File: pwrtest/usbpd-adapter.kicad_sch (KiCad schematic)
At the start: 11 parts, among them J3 USB_C_Receptacle_USB2.0_16P, Q1 AO3400A, U3 IP2721

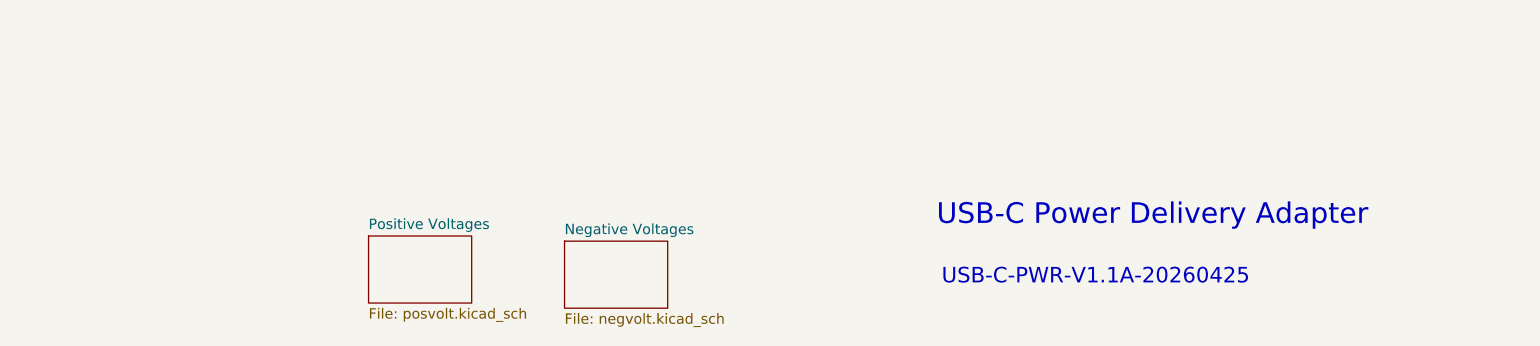
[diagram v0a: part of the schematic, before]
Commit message: adding undervoltage detection circuits
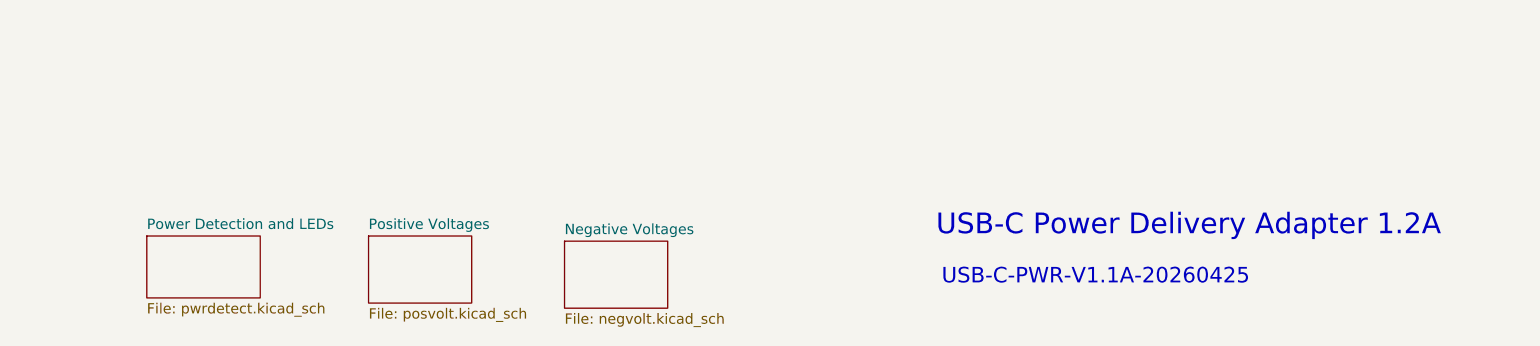
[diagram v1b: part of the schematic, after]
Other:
- added sheet Power Detection and LEDs (pwrdetect.kicad_sch)
- note added: "USB-C Power Delivery Adapter 1.2A"
- note removed: "USB-C Power Delivery Adapter"
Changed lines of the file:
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@@
 	(generator_version "10.0")
 	(paper "A4")
-	(text "USB-C Power Delivery Adapter\n"
-		(exclude_from_sim no)
-		(at 213.995 170.18 0)
+	(text "USB-C Power Delivery Adapter 1.2A\n"
+		(exclude_from_sim no)
+		(at 218.44 171.45 0)
 		(effects
 			(font
@@
 				)
 			)
+		)
+	)
+	(sheet
+		(at 90.17 172.72)
+		(size 13.97 7.62)
+		(exclude_from_sim no)
+		(in_bom yes)
+		(on_board yes)
+		(dnp no)
+		(fields_autoplaced yes)
+		(stroke
+			(width 0.1524)
+			(type solid)
+		)
+		(fill
+			(color 0 0 0 0)
+		)
+		(property "Sheetname" "Power Detection and LEDs"
+			(at 90.17 172.0084 0)
+			(show_name no)
+			(do_not_autoplace no)
+			(effects
+				(font
+					(size 1.27 1.27)
+				)
+				(justify left bottom)
+			)
+		)
+		(property "Sheetfile" "pwrdetect.kicad_sch"
+			(at 90.17 180.9246 0)
+			(show_name no)
+			(do_not_autoplace no)
+			(effects
+				(font
+					(size 1.27 1.27)
+				)
+				(justify left top)
+			)
+		)
+		(instances
+			(project "usbpd-adapter"
+				(path "/4a647462-7ef8-4ca9-abe7-1697e001dd97"
+					(page "4")
+				)
+			)

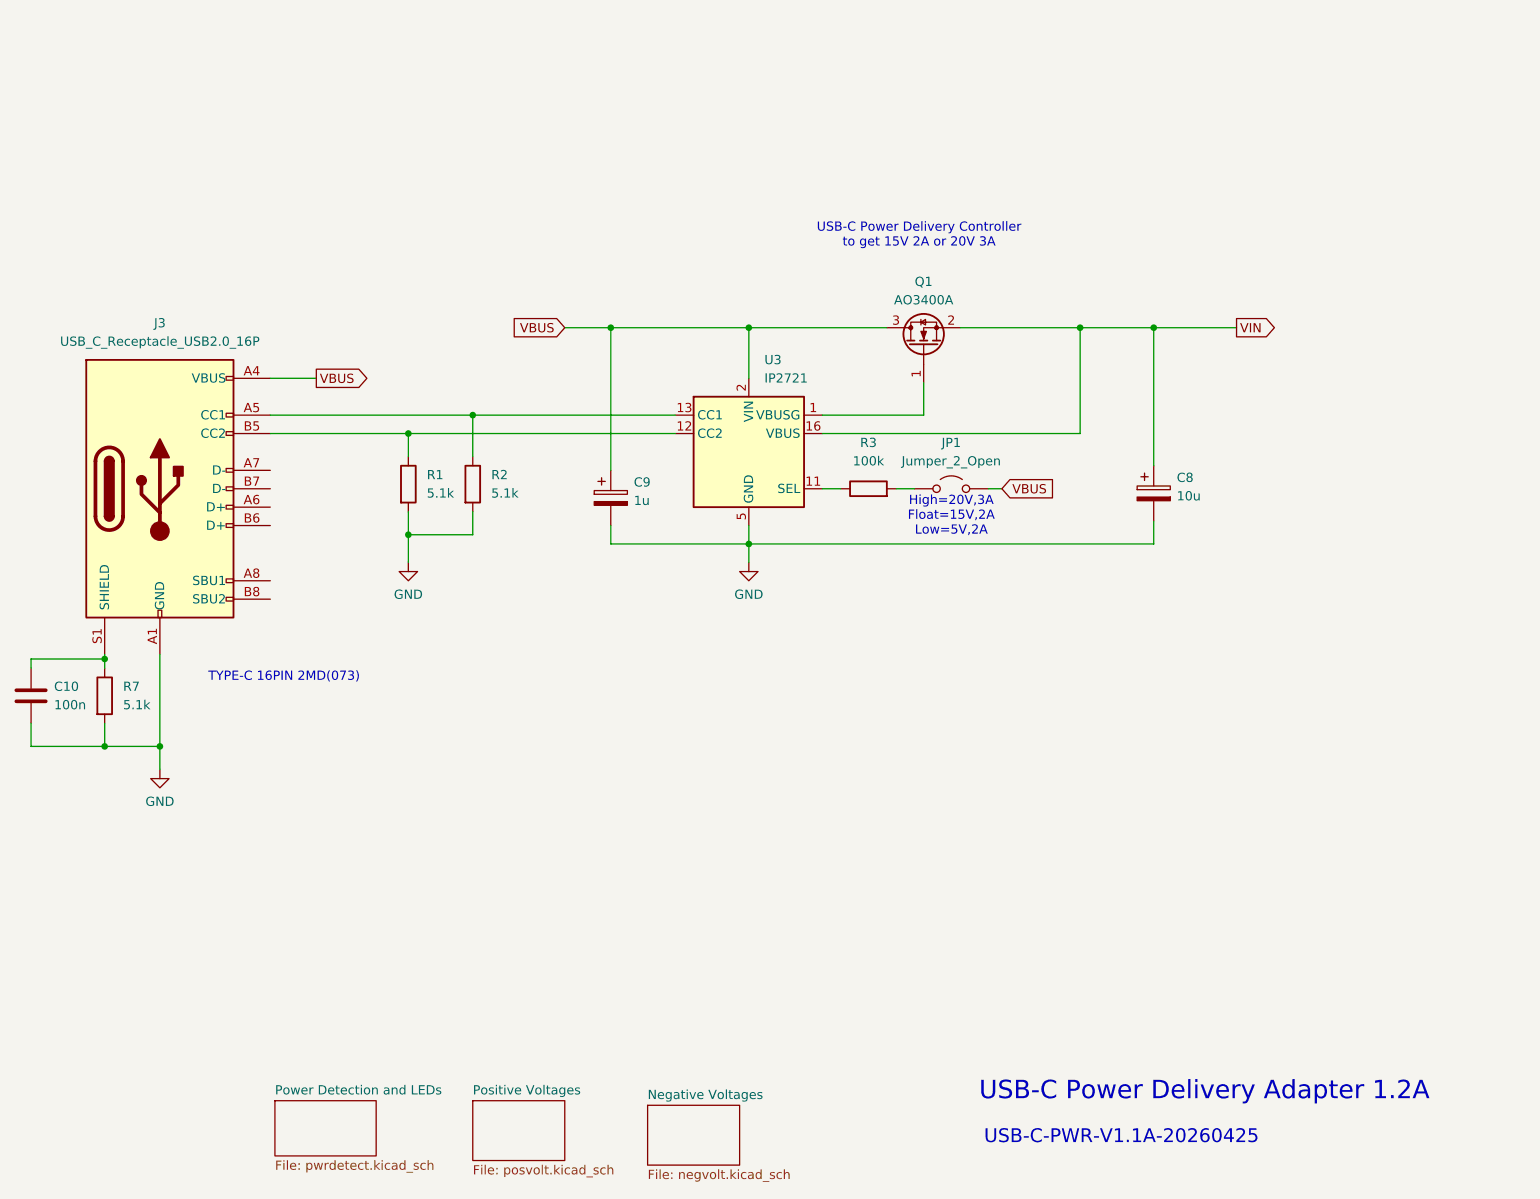
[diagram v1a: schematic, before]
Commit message: new usb controller
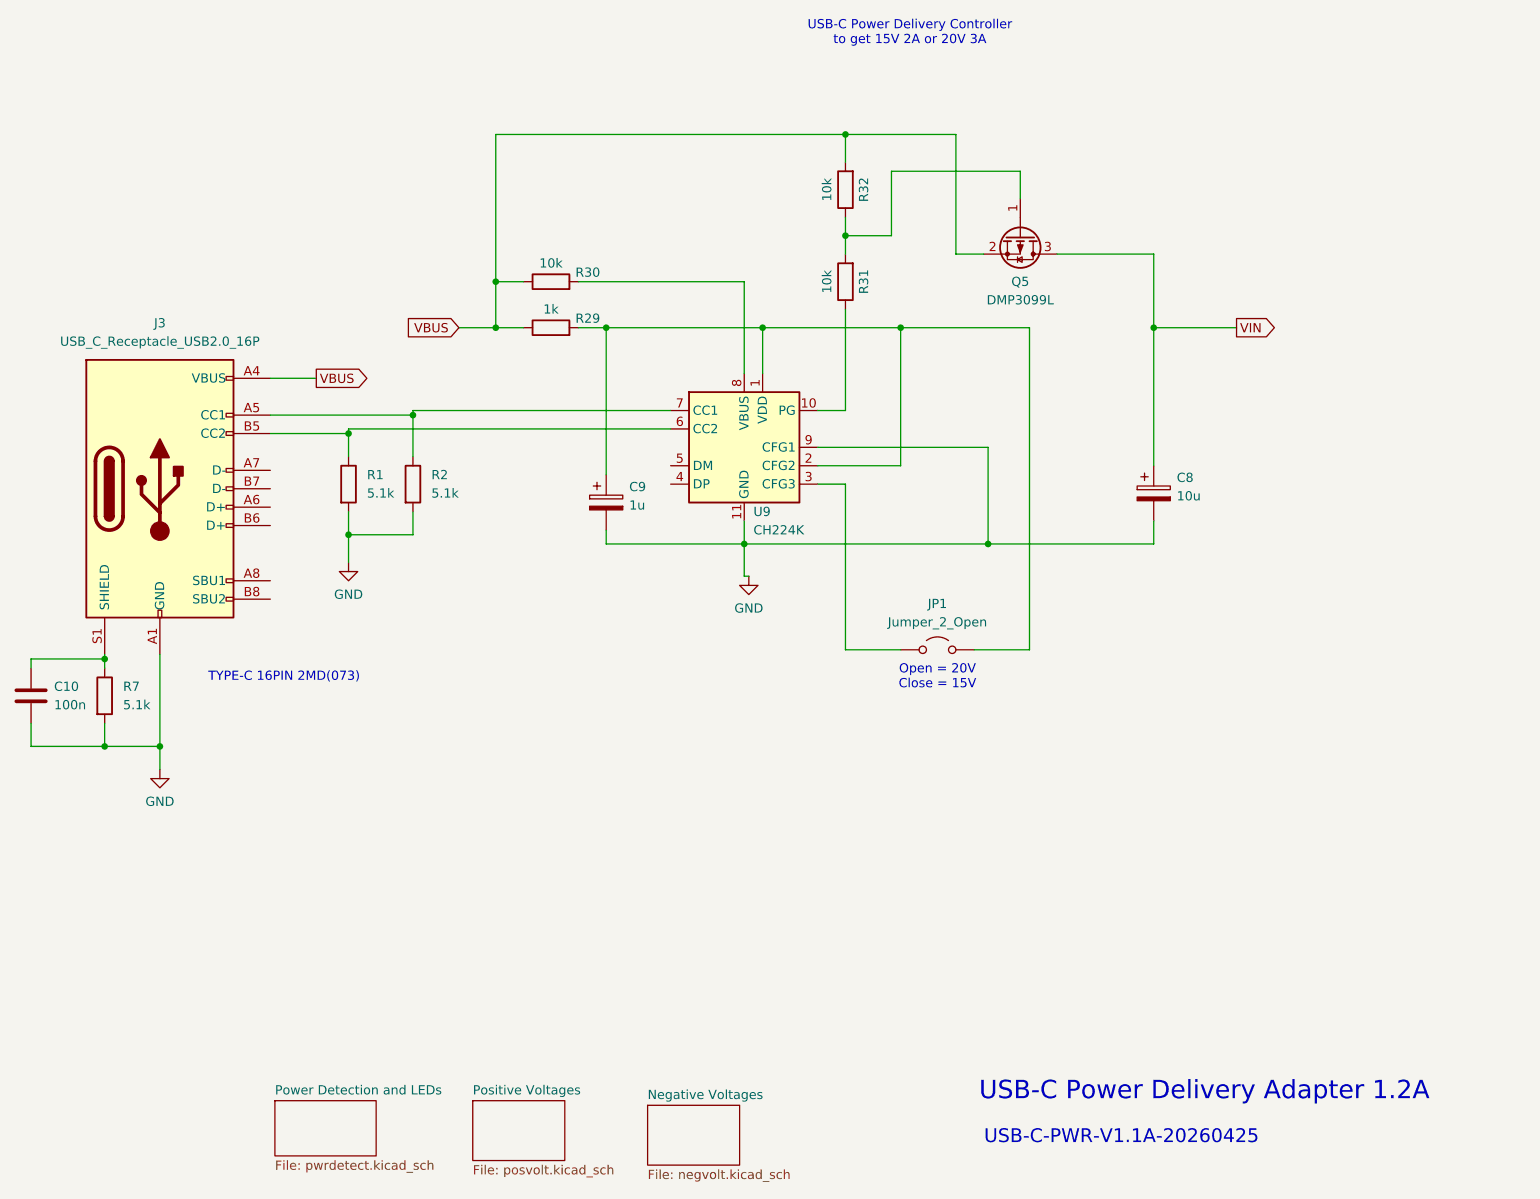
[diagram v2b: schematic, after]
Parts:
- removed Q1: AO3400A, Package_TO_SOT_SMD:SOT-23, symbol Transistor_FET:AO3400A
- removed R3: 100k, Resistor_SMD:R_0603_1608Metric_Pad0.98x0.95mm_HandSolder, symbol Device:R
- removed U3: IP2721, Package_SO:TSSOP-16_4.4x5mm_P0.65mm, symbol Interface_USB:IP2721
- added Q5: DMP3099L, Package_TO_SOT_SMD:SOT-23, symbol Transistor_FET:DMP3099L
- added R29: 1k, Resistor_SMD:R_0603_1608Metric_Pad0.98x0.95mm_HandSolder, symbol Device:R
- added R30, R31, R32: 10k, Resistor_SMD:R_0603_1608Metric_Pad0.98x0.95mm_HandSolder, symbol Device:R
- added U9: CH224K, Package_SO:SSOP-10-1EP_3.9x4.9mm_P1mm_EP2.1x3.3mm, symbol Interface_USB:CH224K
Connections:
- net GND: now also U9.11 (GND), U9.9 (CFG1)
- net VBUS: now also Q5.2 (S), R29.1, R30.1, R32.2; no longer C9.1, JP1.2 (B)
- net VIN: now also Q5.3 (D)
- net at JP1.1 (A): now also U9.3 (CFG3)
- net at J3.B5 (CC2), R1.1: now also U9.6 (CC2)
- net at J3.A5 (CC1), R2.1: now also U9.7 (CC1)
- new net: C9.1, JP1.2 (B), R29.2, U9.1 (VDD), U9.2 (CFG2)
- new net: Q5.1 (G), R31.2, R32.1
- new net: R30.2, U9.8 (VBUS)
- new net: R31.1, U9.10 (PG)
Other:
- note added: "Open = 20V Close = 15V"
- note removed: "High=20V,3A Float=15V,2A Low=5V,2A"
- moved on the sheet: C9, JP1, R1, R2

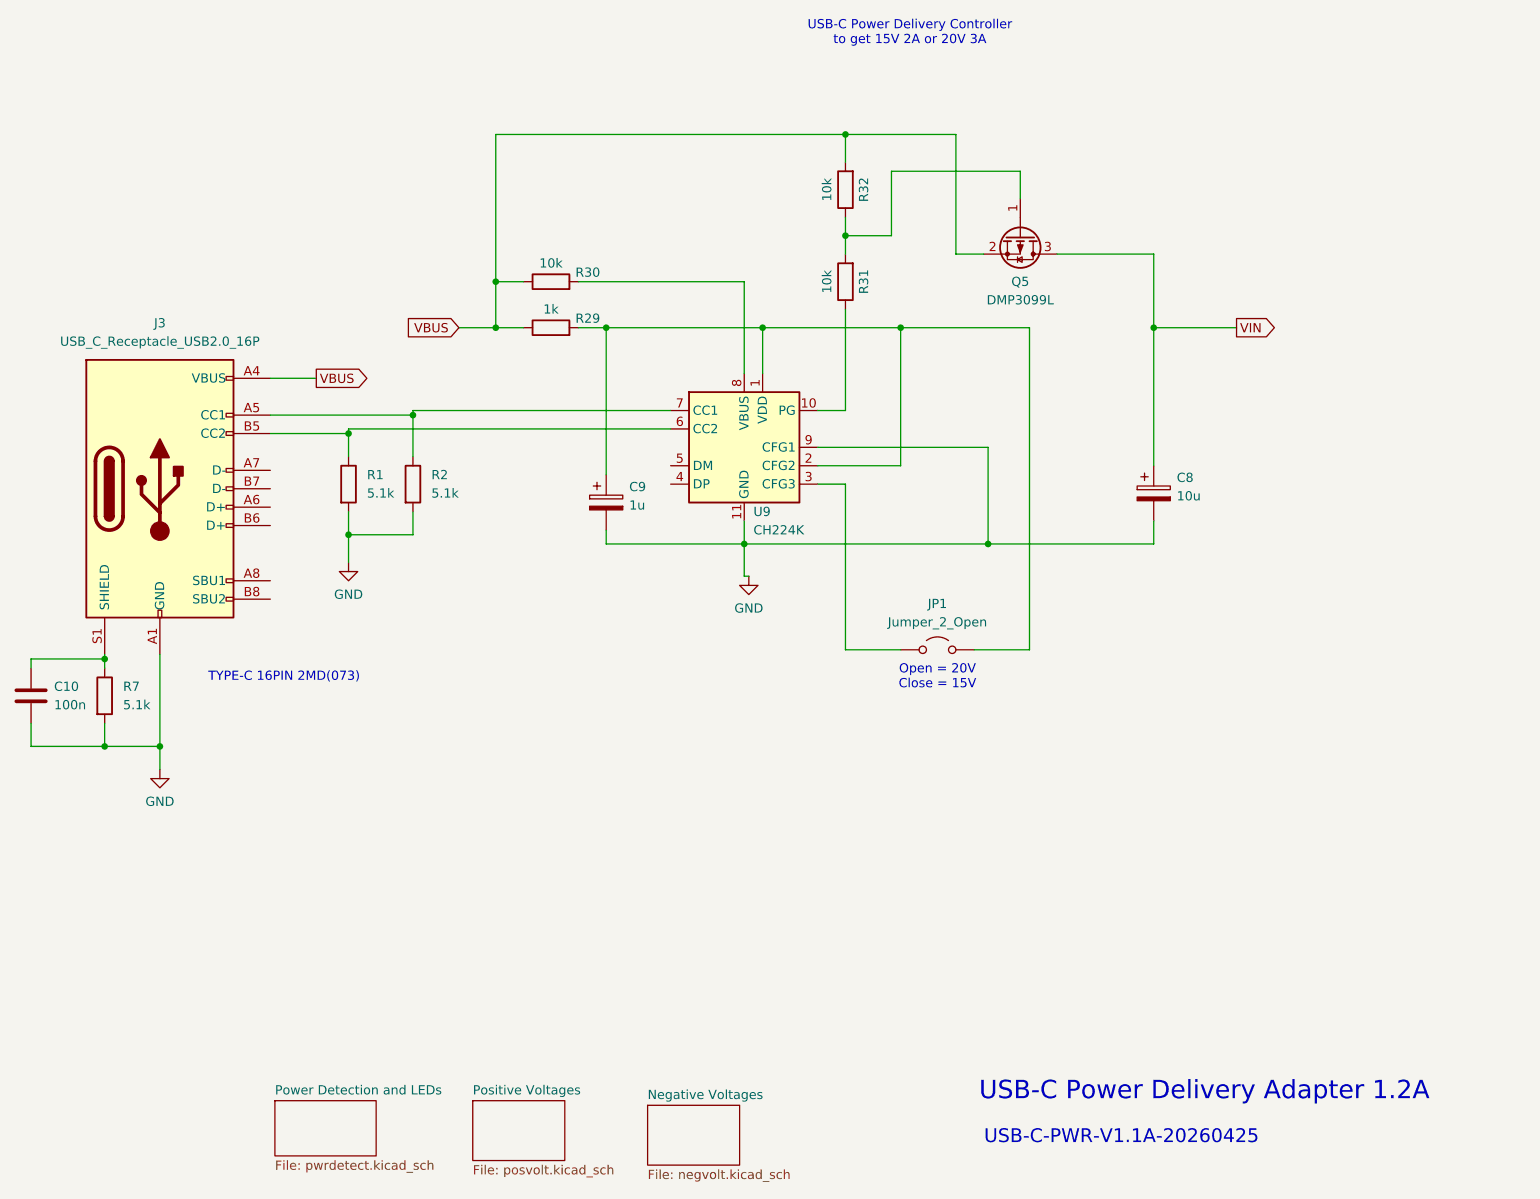
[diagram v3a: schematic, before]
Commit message: updated schematics (untested)
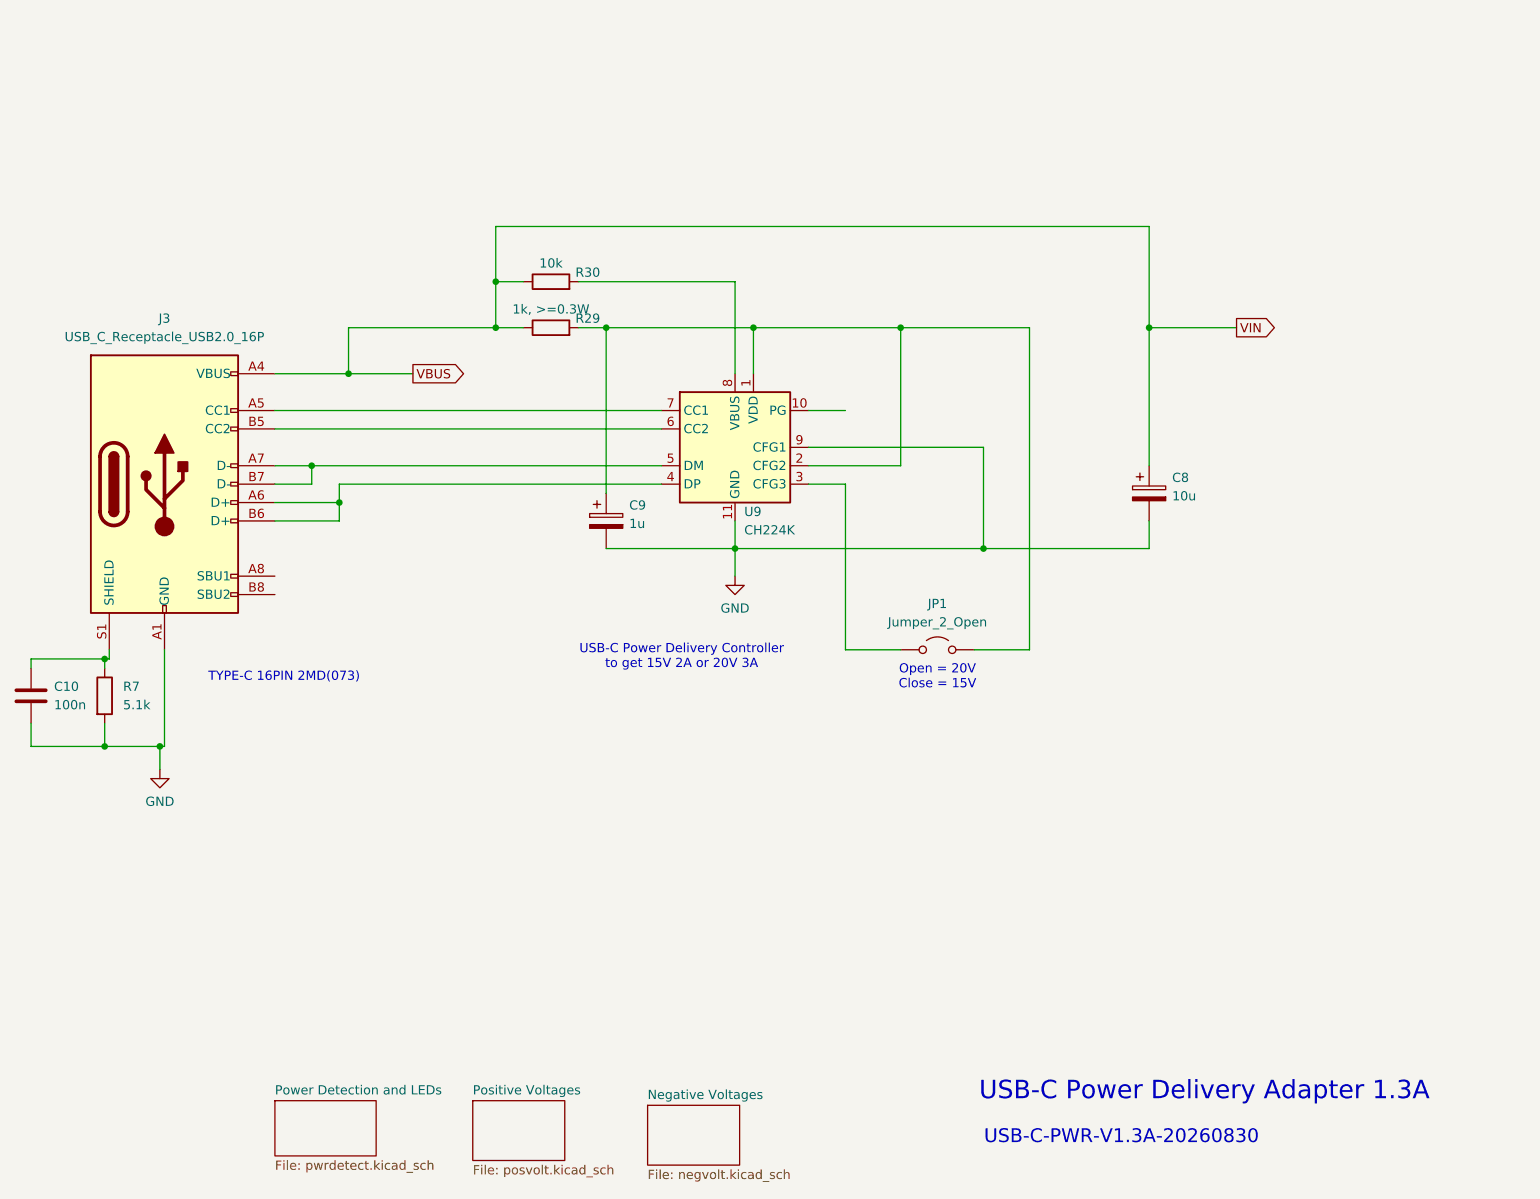
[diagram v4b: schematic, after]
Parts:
- removed Q5: DMP3099L, Package_TO_SOT_SMD:SOT-23, symbol Transistor_FET:DMP3099L
- removed R1, R2: 5.1k, Resistor_SMD:R_0603_1608Metric_Pad0.98x0.95mm_HandSolder, symbol Device:R
- removed R31, R32: 10k, Resistor_SMD:R_0603_1608Metric_Pad0.98x0.95mm_HandSolder, symbol Device:R
- R29: value 1k -> 1k, >=0.3W; LCSC C21190 -> (none)
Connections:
- net VIN is gone; now on net VBUS: C8.1
- net at J3.A6 (D+): now also J3.B6 (D+), U9.4 (DP)
- net at J3.A7 (D-): now also J3.B7 (D-), U9.5 (DM)
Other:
- note added: "USB-C Power Delivery Adapter 1.3A"
- note added: "USB-C-PWR-V1.3A-20260830"
- note removed: "USB-C Power Delivery Adapter 1.2A"
- note removed: "USB-C-PWR-V1.1A-20260425"
- moved on the sheet: C8, C9, J3, U9

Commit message: usb pd updated
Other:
- note added: "USB-C Power Delivery Adapter 1.3B"
- note removed: "USB-C Power Delivery Adapter 1.3A"
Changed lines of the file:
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@@
 	(generator_version "10.0")
 	(paper "A4")
-	(text "USB-C Power Delivery Adapter 1.3A\n"
+	(text "USB-C Power Delivery Adapter 1.3B"
 		(exclude_from_sim no)
 		(at 218.44 171.45 0)

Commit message: add 3.3V and 9V to usb pwr
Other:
- note added: "1.4A: - add 3.3V and 9V"
- note added: "General USB-C based power supply: - 5V 2A (minus what is drawn on 3.3V and 9V) - 12V 1A - -12V Note: - 12V is a linear regulator from Vin - -5V is a linear regulator from -12V - 3.3V and 9V are derived from 5V"
- note added: "USB-C Power Delivery Adapter 1.4A"
- note removed: "USB-C Power Delivery Adapter 1.3B"
- moved on the sheet: C10, C8, C9, J3, JP1, R29, R30, R7, U9
